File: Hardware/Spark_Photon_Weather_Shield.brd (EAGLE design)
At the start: 68.6 x 36.8 mm, 39 parts, among them U2 3.3V MIC5219, U3 ALS-PT19, U4 MPL3115A2LGA8, U5 HTU21D

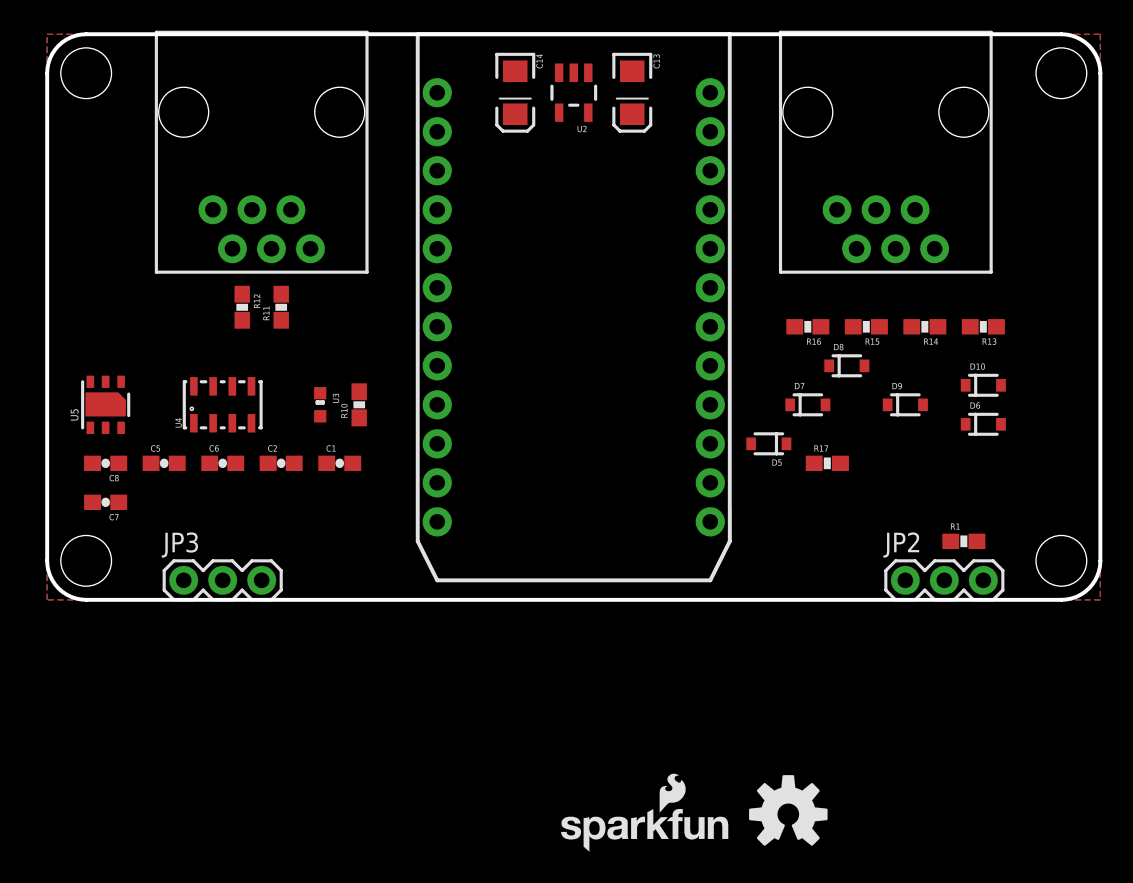
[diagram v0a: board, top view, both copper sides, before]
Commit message: Adding I2C header
Adding I2C header to connect any I2C peripherals desired to enhance the
weather station.
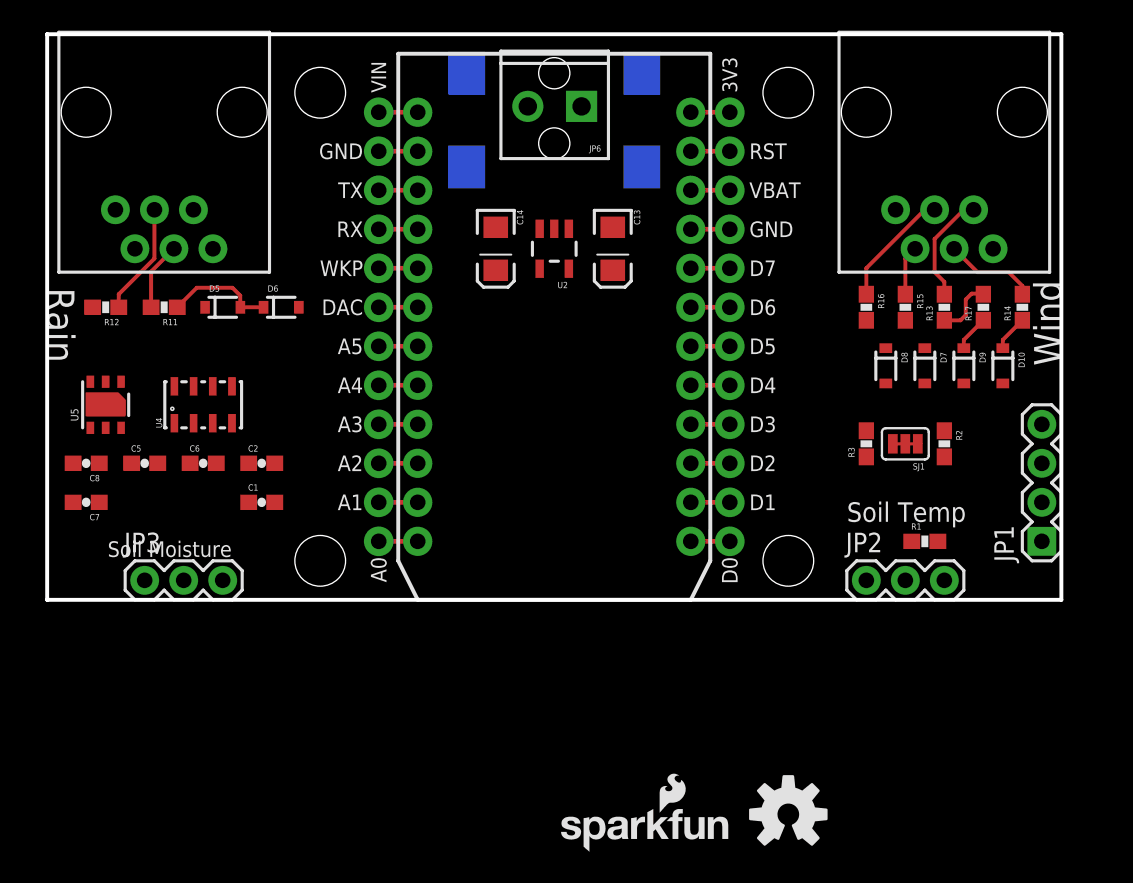
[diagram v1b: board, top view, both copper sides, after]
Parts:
- removed R10: 10K, SparkFun-Passives:0603-RES
- removed STANDOFF1, STANDOFF2, STANDOFF3, STANDOFF4: STAND-OFF, SparkFun-Electromechanical:STAND-OFF
- removed U3: ALS-PT19, SparkFun-Sensors:ALS-PT19
- added JP4: SPARK_PHOTONTEMPLATE, template_temp:SPARK_PHOTON_TEMPLATE
- added JP5: 5.5x2.1mm Barrel, SparkFun-Connectors:POWER_JACK_SMD
- added JP6: M023.5MM, SparkFun-Connectors:SCREWTERMINAL-3.5MM-2
- added R2, R3: 10K, SparkFun-Resistors:0603-RES
- added SJ1: (no value), SparkFun-Passives:PAD-JUMPER-3-3OF3_NC_BY_TRACE_YES_SILK_FULL_BOX
- JP1: value SPARK_PHOTON -> (none); device template_temp:SPARK_PHOTON -> SparkFun-Connectors:1X04
- moved D6 46.4 mm to (15.2, 19.1)
- moved JP1 40.7 mm to (64.8, 3.81), turned to 90 degrees
- moved D5 36.7 mm to (11.4, 19.1), turned to 0 degrees
- moved R17 14.4 mm to (61.0, 19.1), turned to 90 degrees
- moved C13 10.2 mm to (36.8, 22.9)
- moved C14 10.2 mm to (29.2, 22.9)
- moved U2 10.2 mm to (33.0, 22.9)
- moved R12 8.89 mm to (3.81, 19.1), turned to 180 degrees
- moved D7 8.03 mm to (57.1, 15.2), turned to 270 degrees
- moved R11 7.62 mm to (7.62, 19.1), turned to 180 degrees
- moved R14 6.48 mm to (63.5, 19.1), turned to 90 degrees
- moved JP9-DNP 6.35 mm to (12.7, 31.8)
- moved C1 5.68 mm to (14.0, 6.35)
- moved D9 4.58 mm to (59.7, 15.2), turned to 270 degrees
- moved R16 4.02 mm to (53.3, 19.1), turned to 270 degrees
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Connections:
- new net N$3: R3.2, SJ1.3
- new net N$6: R2.2, SJ1.1
- new net SOIL_MOIST: JP3.2, JP4.10, JP4.A2
- net 3.3V: now also JP4.24, JP4.3V3; no longer JP1.24, U3.C
- net GND: now also JP1.4, JP3.1, JP4.2, JP4.21, JP4.GND@0, JP4.GND@2; no longer JP1.2, JP1.21, R10.1
- net LIGHT: now also JP4.11, JP4.A1; no longer JP1.11, R10.2, U3.E
- net RAIN: now also JP4.15, JP4.D2; no longer JP1.15
- net RAW: now also JP4.1, JP4.VIN; no longer JP1.1
- net RXI: now also JP4.4, JP4.RX; no longer JP1.4
- net SCL: now also JP1.1, JP4.14, JP4.D1, R3.1; no longer JP1.14
- net SDA: now also JP1.2, JP4.13, JP4.D0, R2.1; no longer JP1.13
- net SOIL_TEMP: now also JP4.17, JP4.D4, R1.2; no longer JP1.17, R1.1
- net TXO: now also JP4.3, JP4.TX; no longer JP1.3
- net VCC: now also JP1.3, JP3.3, R1.1, SJ1.2; no longer R1.2
- net WDIR: now also JP4.12, JP4.A0; no longer JP1.12
- net WSPEED: now also JP4.16, JP4.D3; no longer JP1.16
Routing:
- net N$13: track 0.00 -> 7.71 mm
- net N$11: track 0.00 -> 7.31 mm
- net N$2: track 0.00 -> 7.19 mm
- net RAIN: track 0.00 -> 7.11 mm
- net N$1: track 0.00 -> 5.99 mm
- net N$4: track 0.00 -> 4.43 mm
- net WDIR: track 0.00 -> 3.87 mm
- net N$12: track 0.00 -> 3.22 mm
- net WSPEED: track 0.00 -> 2.34 mm
- net 5V: track 0.00 -> 2.34 mm
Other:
- board size 68.6 x 36.8 mm -> 66 x 36.8 mm
- board text added: "Rain"
- board text added: "Soil Moisture"
- board text added: "Soil Temp"
- board text added: "Wind"

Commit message: Major Routing - Close to Proto
Major Routing - Close to Proto. added lots of silk and jumper features.
Finished routing.
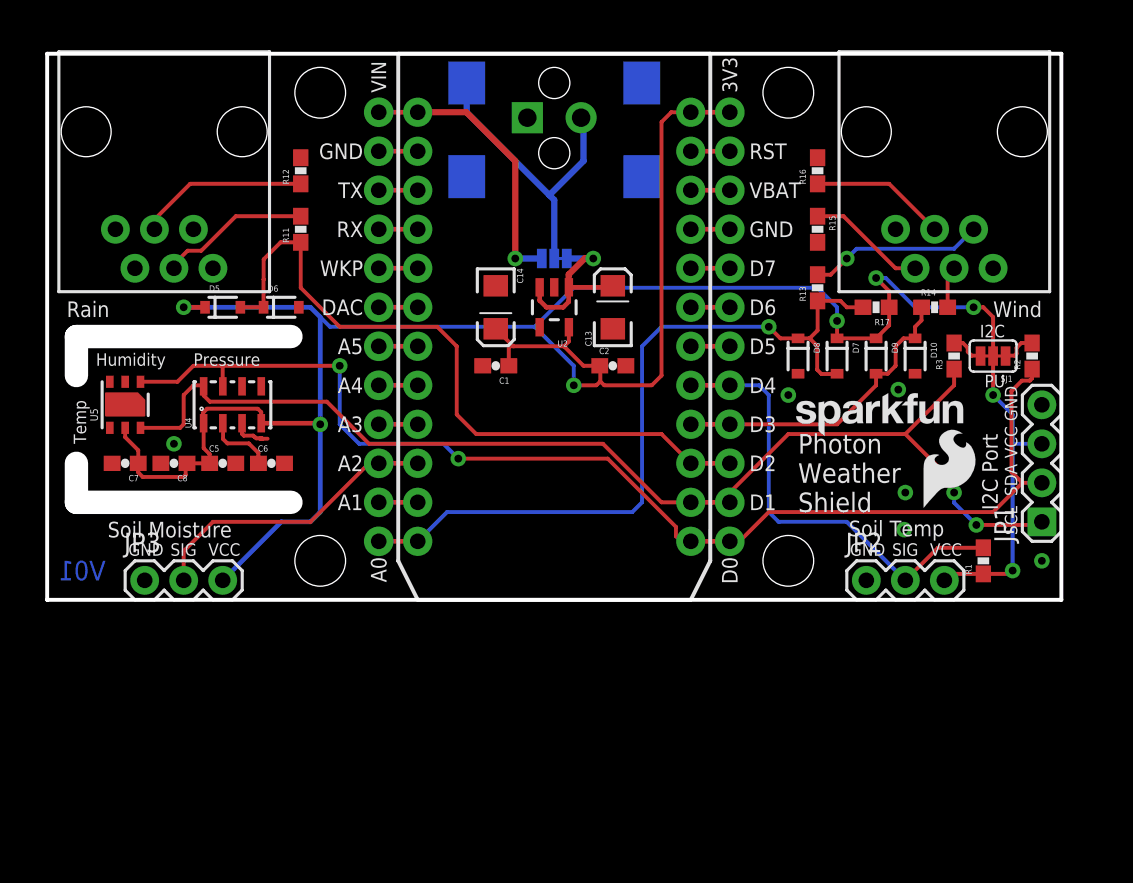
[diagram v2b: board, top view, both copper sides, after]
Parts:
- removed LOGO2: SFE_LOGO_NAME_FLAME.1_INCH, SparkFun-Aesthetics:SFE_LOGO_NAME_FLAME_.1
- added LOGO3: SFE_LOGO_NAME.1_INCH, SparkFun-Aesthetics:SFE_LOGO_NAME_.1
- added LOGO4: SFE_LOGO_FLAME.2_INCH, SparkFun-Aesthetics:SFE_LOGO_FLAME_.2
- added SJ2: (no value), SparkFun-Passives:PAD-JUMPER-3-2OF3_NC_BY_TRACE_YES_SILK_FULL_BOX
- added U$1: (no value), SparkFun-Aesthetics:SFE_LOGO_NAME_FLAME_.1
- moved LOGO1 29.1 mm to (33.0, 10.8), flipped to the bottom
- moved C2 23.7 mm to (36.8, 15.2)
- moved C1 17.6 mm to (29.2, 15.2), turned to 180 degrees
- moved R12 15.5 mm to (16.5, 27.9), turned to 90 degrees
- moved R11 10.2 mm to (16.5, 24.1), turned to 90 degrees
- moved R16 9.44 mm to (50.2, 27.9), turned to 90 degrees
- moved R13 8.35 mm to (50.2, 20.3)
- moved R2 8.08 mm to (64.1, 15.9), turned to 90 degrees
- moved R3 8.08 mm to (59.1, 15.9)
- moved SJ1 8.08 mm to (61.6, 15.9)
- moved R15 7.65 mm to (50.2, 24.1)
- moved FRAME2 7.62 mm to (14.0, -10.2)
- moved R17 6.98 mm to (54.0, 19.1), turned to 180 degrees
- moved D10 5.75 mm to (56.5, 15.9)
- moved D7 5.75 mm to (51.4, 15.9)
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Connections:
- removed net 5V: D5.1, D7.1, D9.1, R17.1
- removed net VCC: JP1.3, JP2.3, JP3.3, R1.1, SJ1.2
- new net PHOTON_VIN: JP4.1, JP4.VIN, SJ2.1
- new net VREG_VIN: C13.A, SJ2.3, U2.1, U2.3
- net 3.3V: now also D5.1, D7.1, D9.1, JP1.3, JP2.3, JP3.3, R1.1, R17.1, SJ1.2
- net GND: now also JP5.GND, JP5.P$4, JP6.1
- net RAW: now also JP5.VIN0, JP6.2, SJ2.2; no longer C13.A, JP4.1, JP4.VIN, U2.1, U2.3
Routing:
- net 3.3V: track 0.00 -> 171.0 mm, vias 0 -> 8
- net SDA: track 0.00 -> 75.4 mm, vias 0 -> 2
- net SCL: track 0.00 -> 73.0 mm, vias 0 -> 2
- net WDIR: track 3.87 -> 47.0 mm, vias 0 -> 1
- net RAIN: track 7.11 -> 43.2 mm
- net SOIL_TEMP: track 0.00 -> 27.1 mm
- net RAW: track 0.00 -> 19.8 mm
- net SOIL_MOIST: track 0.00 -> 17.0 mm
- net PHOTON_VIN: track 0.00 -> 15.7 mm, vias 0 -> 1
- net WSPEED: track 2.34 -> 17.8 mm
- net VREG_VIN: track 0.00 -> 11.5 mm, vias 0 -> 1
- net N$4: track 4.43 -> 9.81 mm
- net N$5: track 0.00 -> 4.86 mm
- net N$12: track 3.22 -> 7.75 mm
- net N$2: track 7.19 -> 11.4 mm, vias 0 -> 1
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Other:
- board size 66 x 36.8 mm -> 66 x 35.6 mm
- board text added: "GND"
- board text added: "Humidity"
- board text added: "I2C"
- board text added: "I2C Port"
- board text added: "Joel Bartlett"
- board text added: "PU"
- board text added: "Photon"
- board text added: "Power Select"
- board text added: "Pressure"
- board text added: "RAW"
- board text added: "SCL"
- board text added: "SDA"
- board text added: "SIG"
- board text added: "Shield"
- board text added: "Temp"
- board text added: "V01"
- board text added: "VCC"
- board text added: "VIN"
- board text added: "VREG"
- board text added: "Weather"

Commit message: Final touches before peer review
Ran my own QC checklist and fixed a few minor details such as
fiducials, labeling, more rerouting, etc.
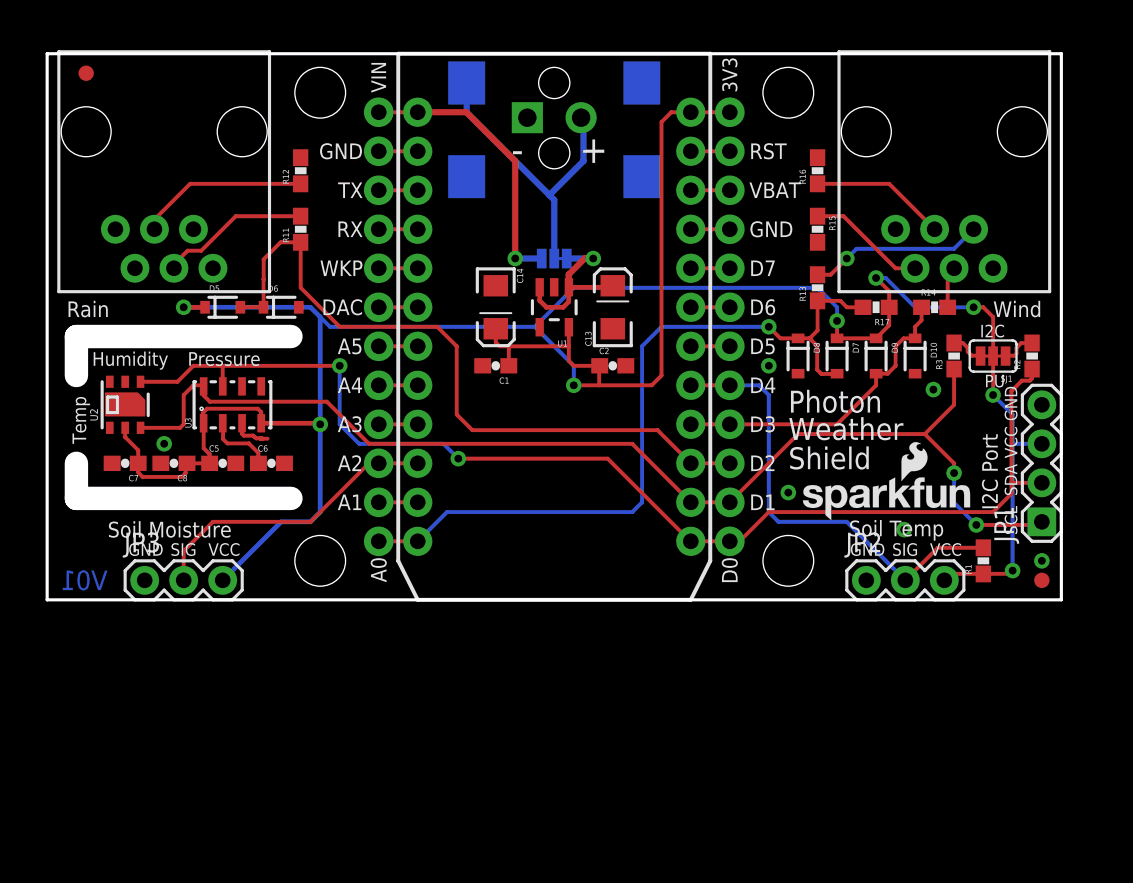
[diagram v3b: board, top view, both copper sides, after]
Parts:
- removed LOGO3: SFE_LOGO_NAME.1_INCH, SparkFun-Aesthetics:SFE_LOGO_NAME_.1
- removed LOGO4: SFE_LOGO_FLAME.2_INCH, SparkFun-Aesthetics:SFE_LOGO_FLAME_.2
- removed U5: HTU21D, SparkFun-Sensors:HTU21D
- added FID1, FID2: FIDUCIAL1X2, SparkFun-Aesthetics:FIDUCIAL-1X2
- added LOGO2: SFE_LOGO_NAME_FLAME.1_INCH, SparkFun-Aesthetics:SFE_LOGO_NAME_FLAME_.1
- added U1: 3.3V MIC5219, SparkFun:SOT23-5
- FRAME2: value FRAME-LETTER -> (none)
- U2: value 3.3V MIC5219 -> HTU21D; device SparkFun:SOT23-5 -> SparkFun-Sensors:HTU21D
- moved U2 28.7 mm to (5.08, 12.7), turned to 90 degrees
- moved FRAME2 3.81 mm to (10.2, -10.2)
- moved U$1 0.74 mm to (39.1, 14.0)
- renumbered JP10-DNP to JP8-DNP, JP9-DNP to JP7-DNP, U4 to U3
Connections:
- removed net VREG_VIN: C13.A, SJ2.3, U2.1, U2.3
- new net VREG: C13.A, SJ2.3, U1.1, U1.3
- net 3.3V: now also U1.5, U2.VDD; no longer U2.5, U5.VDD
- net GND: now also U1.2, U2.7, U2.GND; no longer U2.2, U5.7, U5.GND
- net SCL: now also U2.SCK; no longer U5.SCK
- net SDA: now also U2.DATA; no longer U5.DATA
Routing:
- net VREG_VIN: track 11.5 -> 0.00 mm, vias 1 -> 0
- net VREG: track 0.00 -> 11.5 mm, vias 0 -> 1
- net 3.3V: track 171.0 -> 171.7 mm
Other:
- outline, holes or cut-outs redrawn
- board text added: "+"
- board text added: "-"
- board text added: "P_VIN"
- board text added: "Turn on Milling Layer (46)"
- board text removed: "VIN"
